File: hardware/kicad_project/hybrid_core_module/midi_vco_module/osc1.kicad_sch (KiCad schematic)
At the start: 61 parts, among them Q10 2N7002, Q6 SSM2212, Q8 BF545A, Q9 2N7002, U21 TL074, U22 LM311, U23 TL072

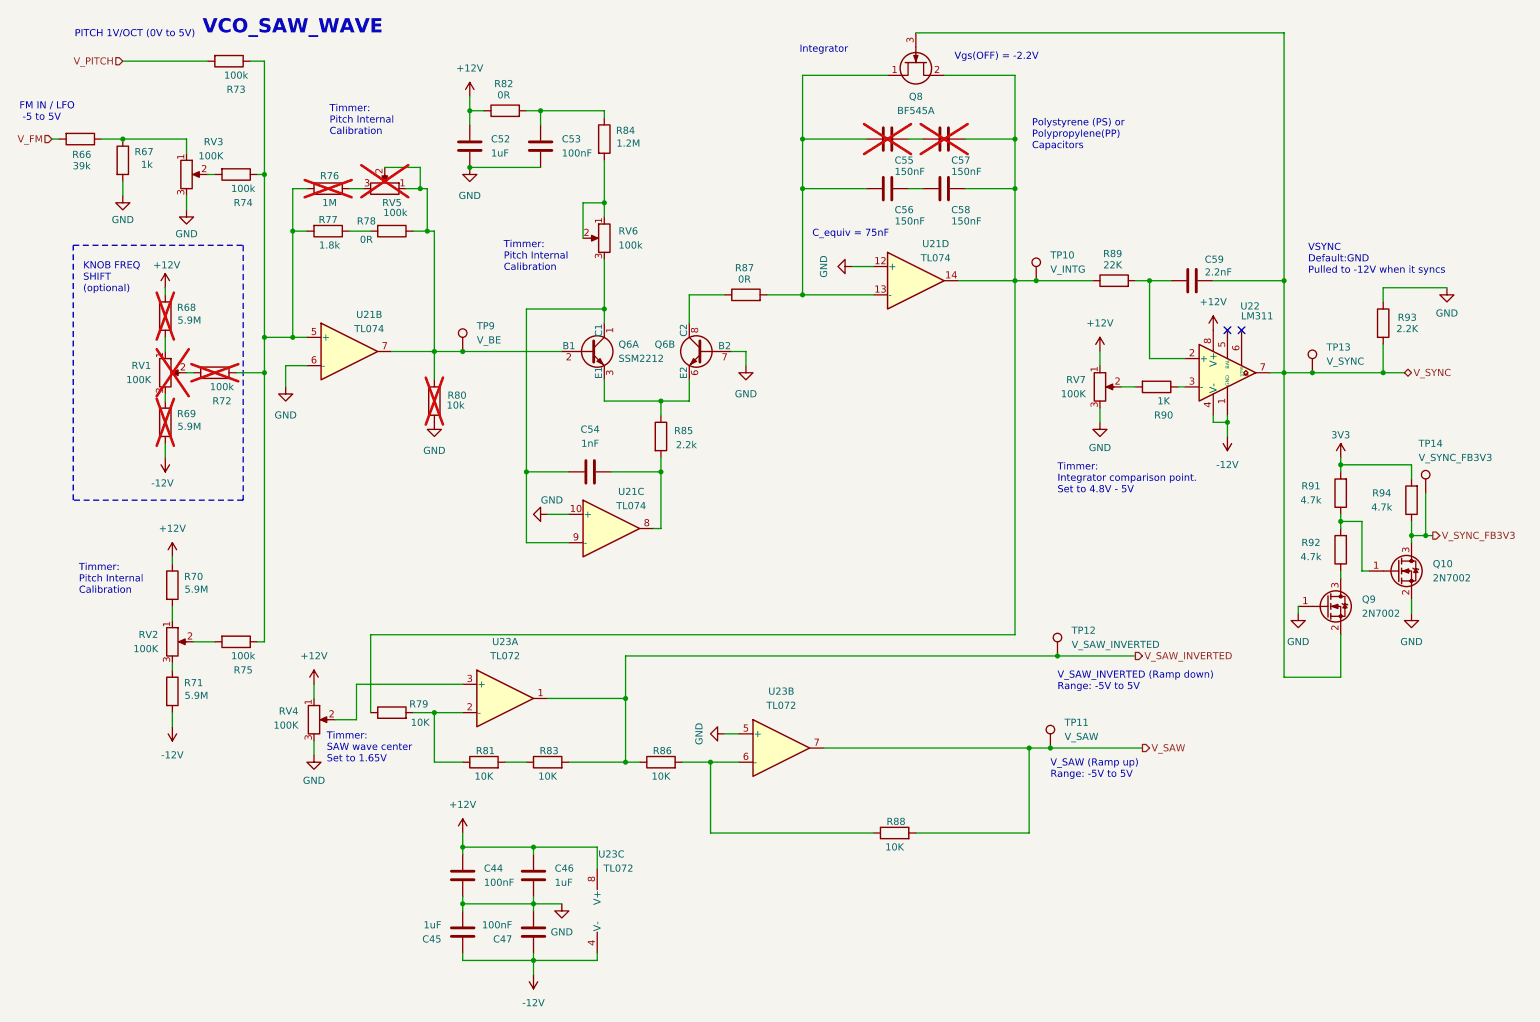
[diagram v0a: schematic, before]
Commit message: Schematic updated. Components Footprint assignment started. Waiting for components mechanical validation before starting layout.
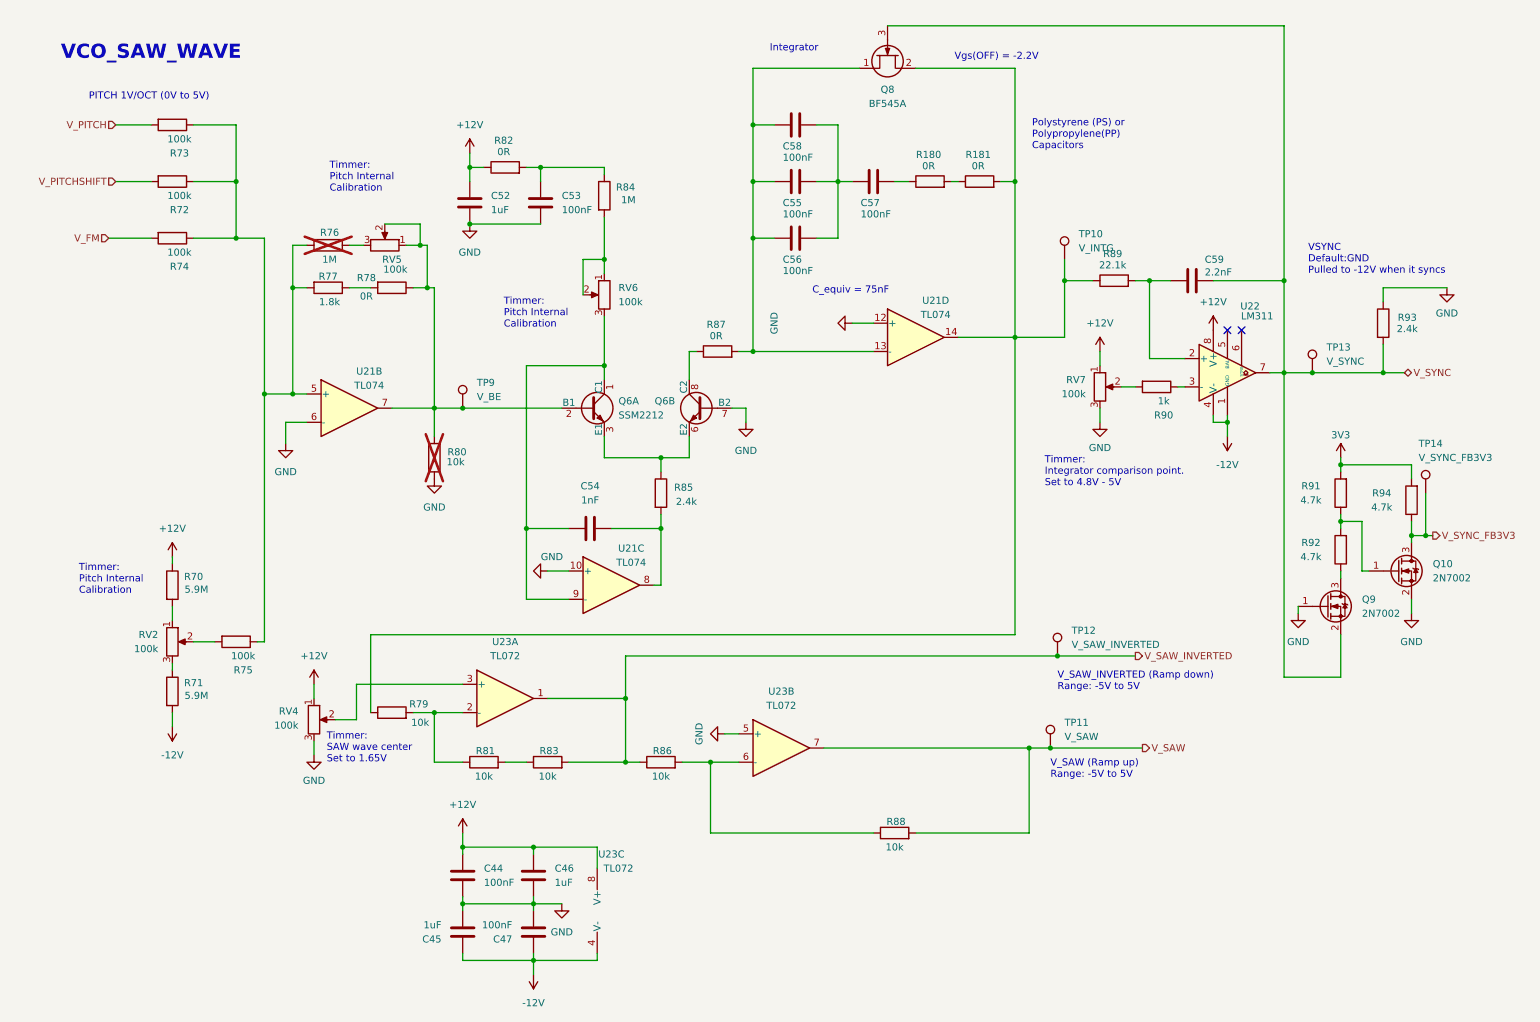
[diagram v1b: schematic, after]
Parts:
- removed R66: 39k, symbol Device:R
- removed R67: 1k, symbol Device:R
- removed R68, R69: 5.9M, symbol Device:R
- removed RV1, RV3: 100K, symbol Device:R_Potentiometer
- added R180, R181: 0R, Resistor_SMD:R_0402_1005Metric, symbol Device:R
- C44, C47, C53: footprint (none) -> Capacitor_SMD:C_0402_1005Metric; Manufacturer (none) -> MURATA; Manufacturer PartNumer (none) -> GRM155R71E104KE14J
- C45, C46, C52: footprint (none) -> Capacitor_SMD:C_0805_2012Metric; Manufacturer (none) -> MURATA; Manufacturer PartNumer (none) -> GRM219R71E105MA88J
- C54: Manufacturer (none) -> MURATA; Manufacturer PartNumer (none) -> GRM155R71E103KA01J
- C55, C57: value 150nF -> 100nF; footprint (none) -> Capacitor_SMD:C_1206_3216Metric; Manufacturer (none) -> KEMET; Manufacturer PartNumer (none) -> GRT31C5C1H104FA02L; now fitted
- C56, C58: value 150nF -> 100nF; footprint (none) -> Capacitor_SMD:C_1206_3216Metric; Manufacturer (none) -> KEMET; Manufacturer PartNumer (none) -> GRT31C5C1H104FA02L
- C59: footprint (none) -> Capacitor_SMD:C_0402_1005Metric; Manufacturer (none) -> MURATA; Manufacturer PartNumer (none) -> GRM155R71H222KA01J
- Q6: footprint (none) -> Package_SO:JEITA_SOIC-8_3.9x4.9mm_P1.27mm; Manufacturer (none) -> ADI; Manufacturer PartNumer (none) -> SSM2212RZ
- R70, R71: footprint (none) -> Resistor_SMD:R_0402_1005Metric; Manufacturer (none) -> YAGEO; Manufacturer PartNumer (none) -> RC0402FR-075M9L
- R72, RV5: footprint (none) -> Resistor_SMD:R_0402_1005Metric; Manufacturer (none) -> YAGEO; Manufacturer PartNumer (none) -> RT0402FRE07100KL; now fitted
- R73, R74, R75, RV6: footprint (none) -> Resistor_SMD:R_0402_1005Metric; Manufacturer (none) -> YAGEO; Manufacturer PartNumer (none) -> RT0402FRE07100KL
- R76: footprint (none) -> Resistor_SMD:R_0402_1005Metric; Manufacturer (none) -> YAGEO; Manufacturer PartNumer (none) -> RE0402BRE071ML
- R77: footprint (none) -> Resistor_SMD:R_0402_1005Metric; Manufacturer (none) -> YAGEO; Manufacturer PartNumer (none) -> RT0402BRE071K8L
- R78, R82, R87: footprint (none) -> Resistor_SMD:R_0402_1005Metric; Manufacturer (none) -> YAGEO; Manufacturer PartNumer (none) -> RC0402FR-070RL
- R79, R81, R83, R86, R88: value 10K -> 10k; footprint (none) -> Resistor_SMD:R_0402_1005Metric; Manufacturer (none) -> YAGEO; Manufacturer PartNumer (none) -> RT0402FRE0710KL
- R80: footprint (none) -> Resistor_SMD:R_0402_1005Metric; Manufacturer (none) -> YAGEO; Manufacturer PartNumer (none) -> RT0402FRE0710KL
- R84: value 1.2M -> 1M; footprint (none) -> Resistor_SMD:R_0402_1005Metric; Manufacturer (none) -> YAGEO; Manufacturer PartNumer (none) -> RE0402BRE071ML
- R85: value 2.2k -> 2.4k; footprint (none) -> Resistor_SMD:R_0402_1005Metric; Manufacturer (none) -> YAGEO; Manufacturer PartNumer (none) -> RT0402BRD072K4L
- R89: value 22K -> 22.1k; footprint (none) -> Resistor_SMD:R_0402_1005Metric; Manufacturer (none) -> YAGEO; Manufacturer PartNumer (none) -> RT0402FRE0721KL
- R90: value 1K -> 1k; footprint (none) -> Resistor_SMD:R_0402_1005Metric; Manufacturer (none) -> YAGEO; Manufacturer PartNumer (none) -> RT0402FRE071KL
- R91, R92, R94: footprint (none) -> Resistor_SMD:R_0402_1005Metric; Manufacturer (none) -> YAGEO; Manufacturer PartNumer (none) -> RT0402FRE074K7L
- R93: value 2.2K -> 2.4k; footprint (none) -> Resistor_SMD:R_0402_1005Metric; Manufacturer (none) -> YAGEO; Manufacturer PartNumer (none) -> RT0402BRD072K4L
- RV2, RV4, RV7: value 100K -> 100k; Manufacturer PartNumer (none) -> 3296X-104-LF
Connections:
- net V_FM: now also R74.2
- net at Q8.2 (D), R79.1, R89.1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: now also R181.2; no longer C57.1, C58.1
- net at C55.2, C56.2, Q8.1 (S)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: now also C58.2
- net V_PITCHSHIFT: now reaches R72.2
- net at C55.1, C57.2: now also C56.1, C58.1
- new net: C57.1, R180.1
- new net: R180.2, R181.1
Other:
- note removed: "FM IN / LFO -5 to 5V"
- note removed: "KNOB FREQ SHIFT (optional)"
- moved on the sheet: C52, C53, C54, C58, Q6A, Q6B, Q8, R73, R74, R76, R77, R78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

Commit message: - schematic updated  - PN and footprints added
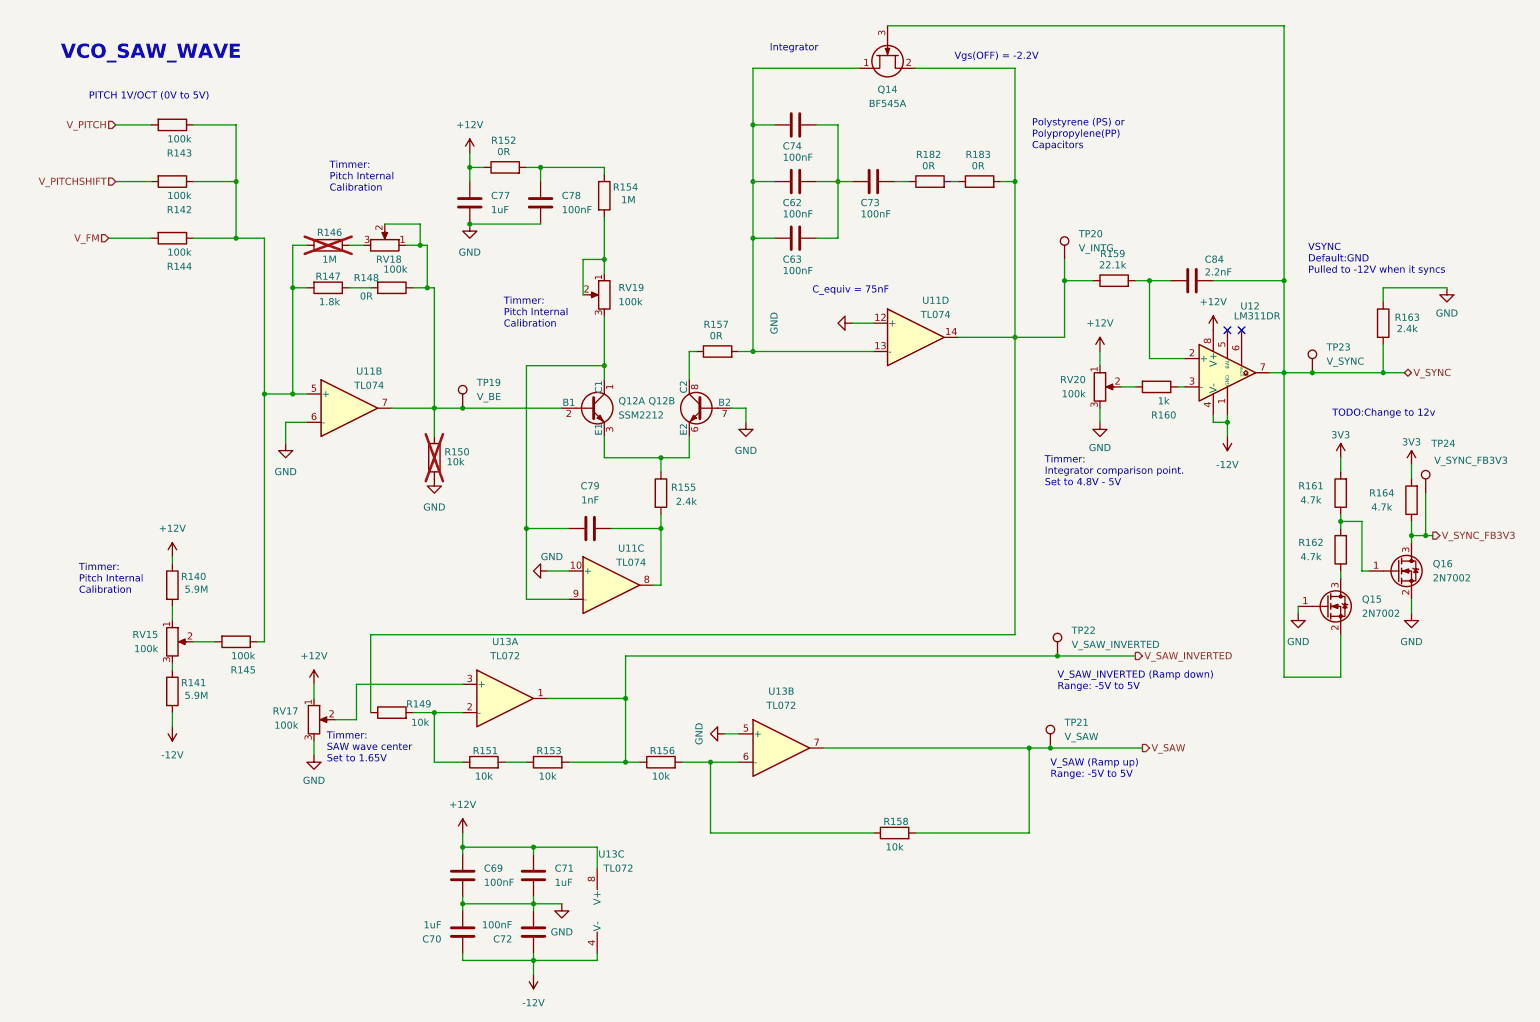
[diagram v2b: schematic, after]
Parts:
- Q14: renamed from Q8; Manufacturer (none) -> onsemi; Manufacturer PartNumer (none) -> MMBFJ108
- Q15: renamed from Q9; Manufacturer (none) -> onsemi; Manufacturer PartNumer (none) -> 2N7002
- Q16: renamed from Q10; Manufacturer (none) -> onsemi; Manufacturer PartNumer (none) -> 2N7002
- RV15: renamed from RV2; footprint (none) -> Potentiometer_THT:Potentiometer_Bourns_3296W_Vertical; Manufacturer (none) -> KESHY; Manufacturer PartNumer 3296X-104-LF -> 3296W-104-LF
- RV17: renamed from RV4; footprint (none) -> Potentiometer_THT:Potentiometer_Bourns_3296W_Vertical; Manufacturer (none) -> KESHY; Manufacturer PartNumer 3296X-104-LF -> 3296W-104-LF
- RV20: renamed from RV7; footprint (none) -> Potentiometer_THT:Potentiometer_Bourns_3296W_Vertical; Manufacturer (none) -> KESHY; Manufacturer PartNumer 3296X-104-LF -> 3296W-104-LF
- U11: renamed from U21; footprint (none) -> Package_SO:SOIC-14_3.9x8.7mm_P1.27mm; Manufacturer (none) -> Texas Instruments
- U12: renamed from U22; value LM311 -> LM311DR; footprint (none) -> Package_SO:SOIC-8_5.3x6.2mm_P1.27mm; Manufacturer (none) -> Texas Instruments; Manufacturer PartNumer (none) -> LM311DR
- U13: renamed from U23; footprint (none) -> Package_SO:SOIC-8_5.3x6.2mm_P1.27mm; Manufacturer (none) -> Texas Instruments; Manufacturer PartNumer (none) -> TL072CDR
- renumbered C55 to C62, C56 to C63, C44 to C69, C45 to C70, C46 to C71, C47 to C72, C57 to C73, C58 to C74, C52 to C77, C53 to C78, C54 to C79, C59 to C84, Q6 to Q12, R70 to R140, R71 to R141, R72 to R142, R73 to R143, R74 to R144, R75 to R145, R76 to R146, R77 to R147, R78 to R148, R79 to R149, R80 to R150, R81 to R151, R82 to R152, R83 to R153, R84 to R154, R85 to R155, R86 to R156, R87 to R157, R88 to R158, R89 to R159, R90 to R160, R91 to R161, R92 to R162, R93 to R163, R94 to R164, R180 to R182, R181 to R183, RV5 to RV18, RV6 to RV19, TP9 to TP19, TP10 to TP20, TP11 to TP21, TP12 to TP22, TP13 to TP23, TP14 to TP24
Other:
- note added: "TODO:Change to 12v"

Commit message: components placement (interface) components placement per section
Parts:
- R182, R183: footprint Resistor_SMD:R_0402_1005Metric -> Resistor_SMD:R_1206_3216Metric
- RV18, RV19: footprint Resistor_SMD:R_0402_1005Metric -> Potentiometer_THT:Potentiometer_Bourns_3296W_Vertical
- TP19, TP20, TP21, TP22, TP23, TP24: footprint (none) -> TestPoint:TestPoint_Pad_1.0x1.0mm
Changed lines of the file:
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@@
 			)
 		)
-		(property "Footprint" ""
+		(property "Footprint" "TestPoint:TestPoint_Pad_1.0x1.0mm"
 			(at 271.78 100.33 0)
 			(effects
@@
 			)
 		)
-		(property "Footprint" ""
+		(property "Footprint" "TestPoint:TestPoint_Pad_1.0x1.0mm"
 			(at 207.01 58.42 0)
 			(effects
@@
 			)
 		)
-		(property "Footprint" ""
+		(property "Footprint" "TestPoint:TestPoint_Pad_1.0x1.0mm"
 			(at 99.06 85.09 0)
 			(effects
@@
 			)
 		)
-		(property "Footprint" ""
+		(property "Footprint" "TestPoint:TestPoint_Pad_1.0x1.0mm"
 			(at 251.46 78.74 0)
 			(effects
@@
 			(project "midi_vco_module"
 				(path "/3378c2b5-f4b3-47f0-8cdf-dba4991b82b5/b5adf1fd-f7fc-415c-86aa-632345bd7954"
-					(reference "#PWR0297")
+					(reference "#PWR0130")
 					(unit 1)
 				)
@@
 			)
 		)
-		(property "Footprint" "Resistor_SMD:R_0402_1005Metric"
+		(property "Footprint" "Potentiometer_THT:Potentiometer_Bourns_3296W_Vertical"
 			(at 80.01 55.88 0)
 			(effects
@@
 			)
 		)
-		(property "Footprint" ""
+		(property "Footprint" "TestPoint:TestPoint_Pad_1.0x1.0mm"
 			(at 205.74 129.54 0)
 			(effects
@@
 			)
 		)
-		(property "Footprint" "Resistor_SMD:R_0402_1005Metric"
+		(property "Footprint" "Resistor_SMD:R_1206_3216Metric"
 			(at 177.8 46.228 90)
 			(effects
@@
 			)
 		)
-		(property "Footprint" "Resistor_SMD:R_0402_1005Metric"
+		(property "Footprint" "Resistor_SMD:R_1206_3216Metric"
 			(at 186.69 46.228 90)
 			(effects
@@
 			)
 		)
-		(property "Footprint" ""
+		(property "Footprint" "TestPoint:TestPoint_Pad_1.0x1.0mm"
 			(at 204.47 146.05 0)
 			(effects
@@
 			)
 		)
-		(property "Footprint" "Resistor_SMD:R_0402_1005Metric"
+		(property "Footprint" "Potentiometer_THT:Potentiometer_Bourns_3296W_Vertical"
 			(at 119.38 64.77 0)
 			(effects

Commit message: - placement done - routing 60%
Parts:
- added C100, C97: 100nF, Capacitor_SMD:C_0402_1005Metric, symbol Device:C
- added C98, C99: 1uF, Capacitor_SMD:C_0805_2012Metric, symbol Device:C
- added R202: 5.1M, Resistor_SMD:R_0402_1005Metric, symbol Device:R
- added R211: 820k, Resistor_SMD:R_0402_1005Metric, symbol Device:R
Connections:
- net +12V: now also C97.1, C99.1, R202.1; no longer RV17.1
- net -12V: now also C100.1, C98.1
- net GND: now also C100.2, C97.2, C98.2, C99.2, R211.2; no longer RV17.3
- new net: R202.2, RV17.1
- new net: R211.1, RV17.3

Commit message: routing continued.
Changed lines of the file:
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@@
 		(lib_id "power:+15V")
 		(at 41.91 111.76 0)
+		(mirror y)
 		(unit 1)
 		(exclude_from_sim no)
@@
 		(on_board yes)
 		(dnp no)
-		(fields_autoplaced yes)
 		(property "Reference" "#PWR0279"
 			(at 41.91 115.57 0)
